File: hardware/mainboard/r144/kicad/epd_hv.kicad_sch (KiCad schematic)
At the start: 33 parts, among them J3 FH34SRJ-24S-0.5SH(50), Q1 IRLML6346TRPBF

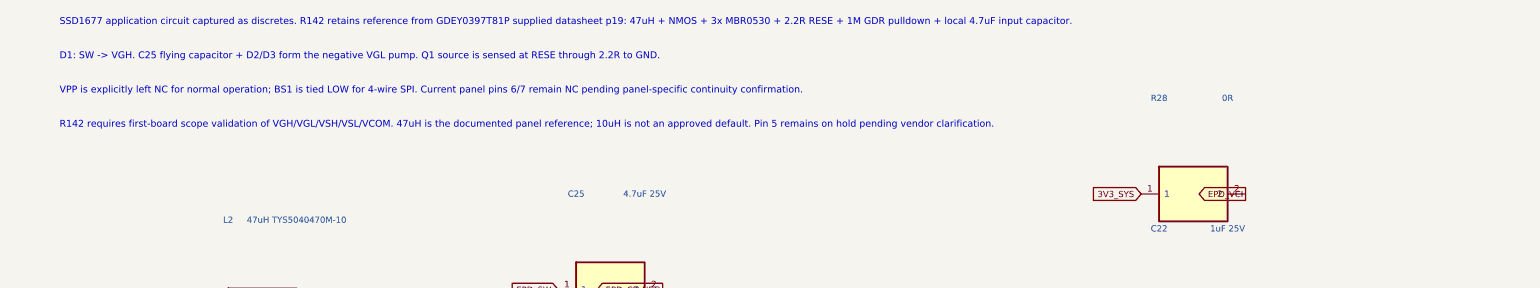
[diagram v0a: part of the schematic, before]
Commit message: R144: synchronize schematic titles and confirmed panel annotation; correct informational divider current
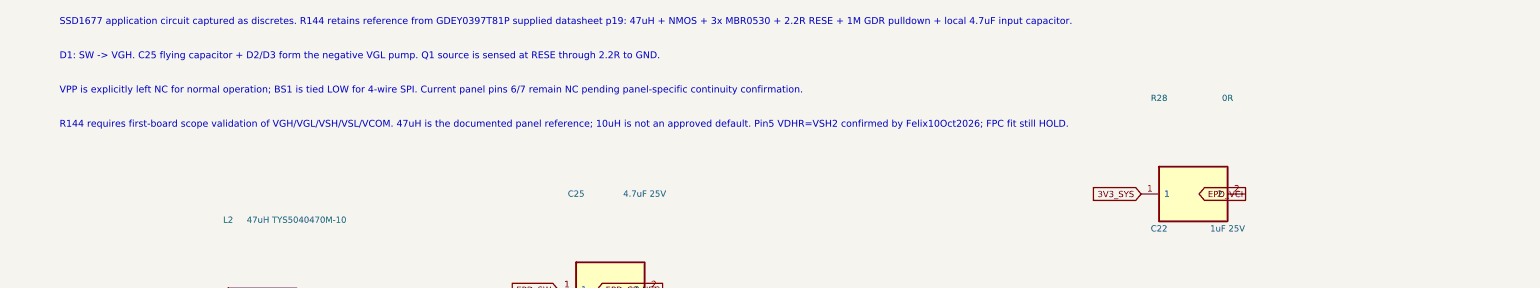
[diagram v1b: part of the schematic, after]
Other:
- note added: "R144 requires first-board scope validation of VGH/VGL/VSH/VSL/VCOM. 47uH is the documented panel reference; 10uH is not an approved default. Pin5 VDHR=VSH2 confirmed by Felix10Oct2026; FPC fit still HOLD."
- note added: "SSD1677 application circuit captured as discretes. R144 retains reference from GDEY0397T81P supplied datasheet p19: 47uH + NMOS + 3x MBR0530 + 2.2R RESE + 1M GDR pulldown + local 4.7uF input capacitor."
- note removed: "R142 requires first-board scope validation of VGH/VGL/VSH/VSL/VCOM. 47uH is the documented panel reference; 10uH is not an approved default. Pin 5 remains on hold pending vendor clarification."
- note removed: "SSD1677 application circuit captured as discretes. R142 retains reference from GDEY0397T81P supplied datasheet p19: 47uH + NMOS + 3x MBR0530 + 2.2R RESE + 1M GDR pulldown + local 4.7uF input capacitor."
- title: ENKU R143 — SSD1677 EPD + HV -> ENKU R144 — SSD1677 EPD + HV
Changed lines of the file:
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@@
 	(paper "A3")
 	(title_block
-		(title "ENKU R143 — SSD1677 EPD + HV")
-		(date "2026-10-14")
+		(title "ENKU R144 — SSD1677 EPD + HV")
+		(date "2026-10-15")
 		(rev "R144 - ENGINEERING / NO FAB")
 		(company "ENKU")
@@
 	(global_label "GND" (shape input) (at 208.28 102.87 0) (effects (font (size 0.9 0.9)) (justify right bottom)))
 	(global_label "GND" (shape input) (at 247.65 102.87 180) (effects (font (size 0.9 0.9)) (justify right bottom)))
-	(text "SSD1677 application circuit captured as discretes. R142 retains reference from GDEY0397T81P supplied datasheet p19: 47uH + NMOS + 3x MBR0530 + 2.2R RESE + 1M GDR pulldown + local 4.7uF input capacitor." (exclude_from_sim no) (at 25 20 0) (effects (font (size 1.0 1.0)) (justify left bottom)))
+	(text "SSD1677 application circuit captured as discretes. R144 retains reference from GDEY0397T81P supplied datasheet p19: 47uH + NMOS + 3x MBR0530 + 2.2R RESE + 1M GDR pulldown + local 4.7uF input capacitor." (exclude_from_sim no) (at 25 20 0) (effects (font (size 1.0 1.0)) (justify left bottom)))
 	(text "D1: SW -> VGH. C25 flying capacitor + D2/D3 form the negative VGL pump. Q1 source is sensed at RESE through 2.2R to GND." (exclude_from_sim no) (at 25 25 0) (effects (font (size 1.0 1.0)) (justify left bottom)))
 	(text "VPP is explicitly left NC for normal operation; BS1 is tied LOW for 4-wire SPI. Current panel pins 6/7 remain NC pending panel-specific continuity confirmation." (exclude_from_sim no) (at 25 30 0) (effects (font (size 1.0 1.0)) (justify left bottom)))
-	(text "R142 requires first-board scope validation of VGH/VGL/VSH/VSL/VCOM. 47uH is the documented panel reference; 10uH is not an approved default. Pin 5 remains on hold pending vendor clarification." (exclude_from_sim no) (at 25 35 0) (effects (font (size 1.0 1.0)) (justify left bottom)))
+	(text "R144 requires first-board scope validation of VGH/VGL/VSH/VSL/VCOM. 47uH is the documented panel reference; 10uH is not an approved default. Pin5 VDHR=VSH2 confirmed by Felix10Oct2026; FPC fit still HOLD." (exclude_from_sim no) (at 25 35 0) (effects (font (size 1.0 1.0)) (justify left bottom)))
 	(symbol (lib_id "ENKU:TESTPOINT") (at 44.45 199.39 0) (unit 1) (exclude_from_sim no) (in_bom no) (on_board yes) (dnp no)
 		(property "Reference" "TP9" (at 44.45 196.85 0) (effects (font (size 0.9 0.9))))
